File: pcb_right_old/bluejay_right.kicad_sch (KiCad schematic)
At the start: 69 parts, among them J2 SJ-43514, U2 MCP23017

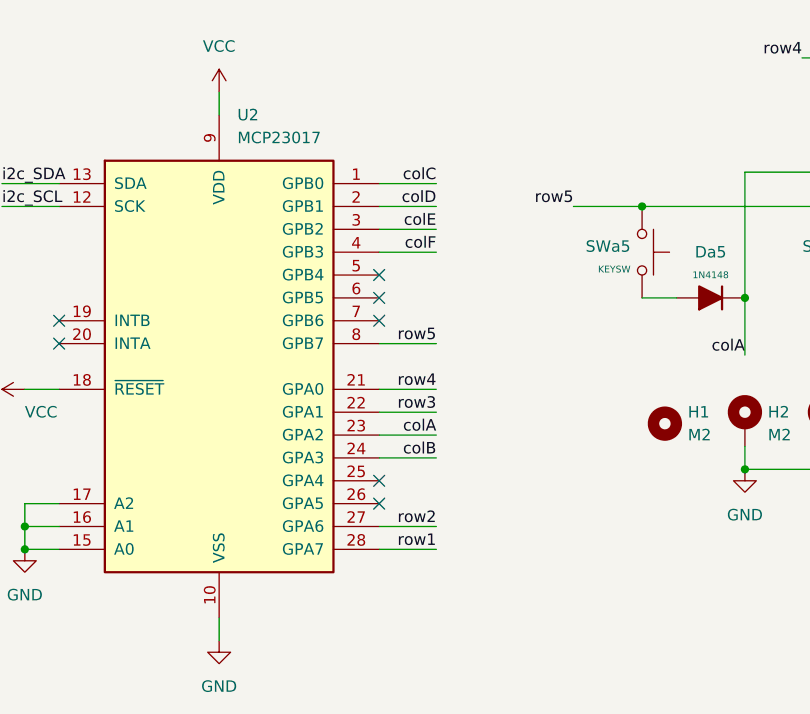
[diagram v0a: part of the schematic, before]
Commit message: Create base pcb
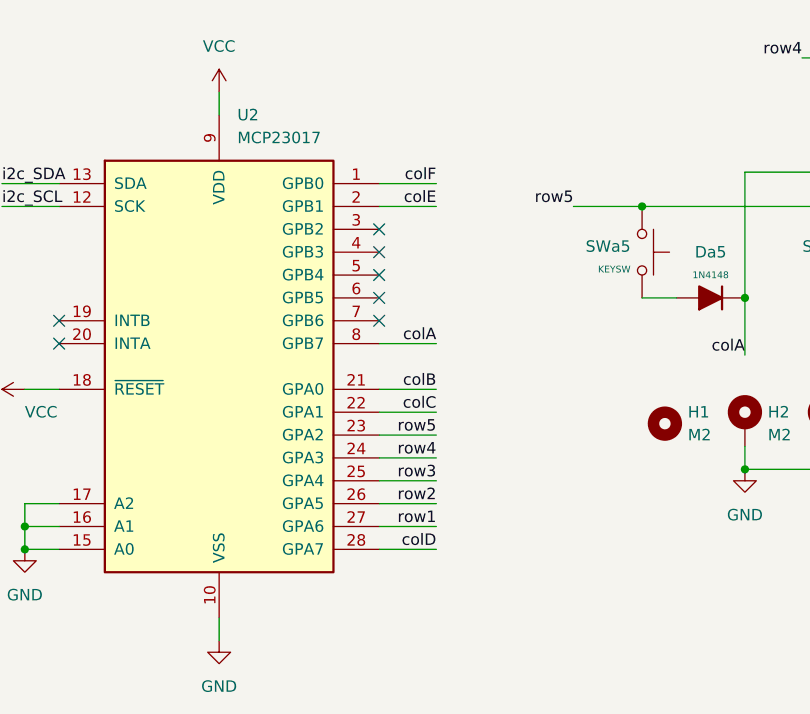
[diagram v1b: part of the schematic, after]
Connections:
- net colA: now also U2.8 (GPB7); no longer U2.23 (GPA2)
- net colB: now also U2.21 (GPA0); no longer U2.24 (GPA3)
- net colC: now also U2.22 (GPA1); no longer U2.1 (GPB0)
- net colD: now also U2.28 (GPA7); no longer U2.2 (GPB1)
- net colE: now also U2.2 (GPB1); no longer U2.3 (GPB2)
- net colF: now also U2.1 (GPB0); no longer U2.4 (GPB3)
- net row1: now also U2.27 (GPA6); no longer U2.28 (GPA7)
- net row2: now also U2.26 (GPA5); no longer U2.27 (GPA6)
- net row3: now also U2.25 (GPA4); no longer U2.22 (GPA1)
- net row4: now also U2.24 (GPA3); no longer U2.21 (GPA0)
- net row5: now also U2.23 (GPA2); no longer U2.8 (GPB7)
